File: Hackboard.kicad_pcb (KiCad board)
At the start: 4 copper layers, 100 x 53.3 mm, 74 parts, among them J1 Conn_01x23_Socket, J2 Micro_SD_Card, J3 Conn_01x32_Socket, J4 Conn_01x08_Socket, J5 Conn_01x02_Pin, J6 USB_C_Receptacle_USB2.0_16P, J7 Barrel_Jack_Switch, Q1 NMOS, Q2 NMOS, Q3 NMOS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

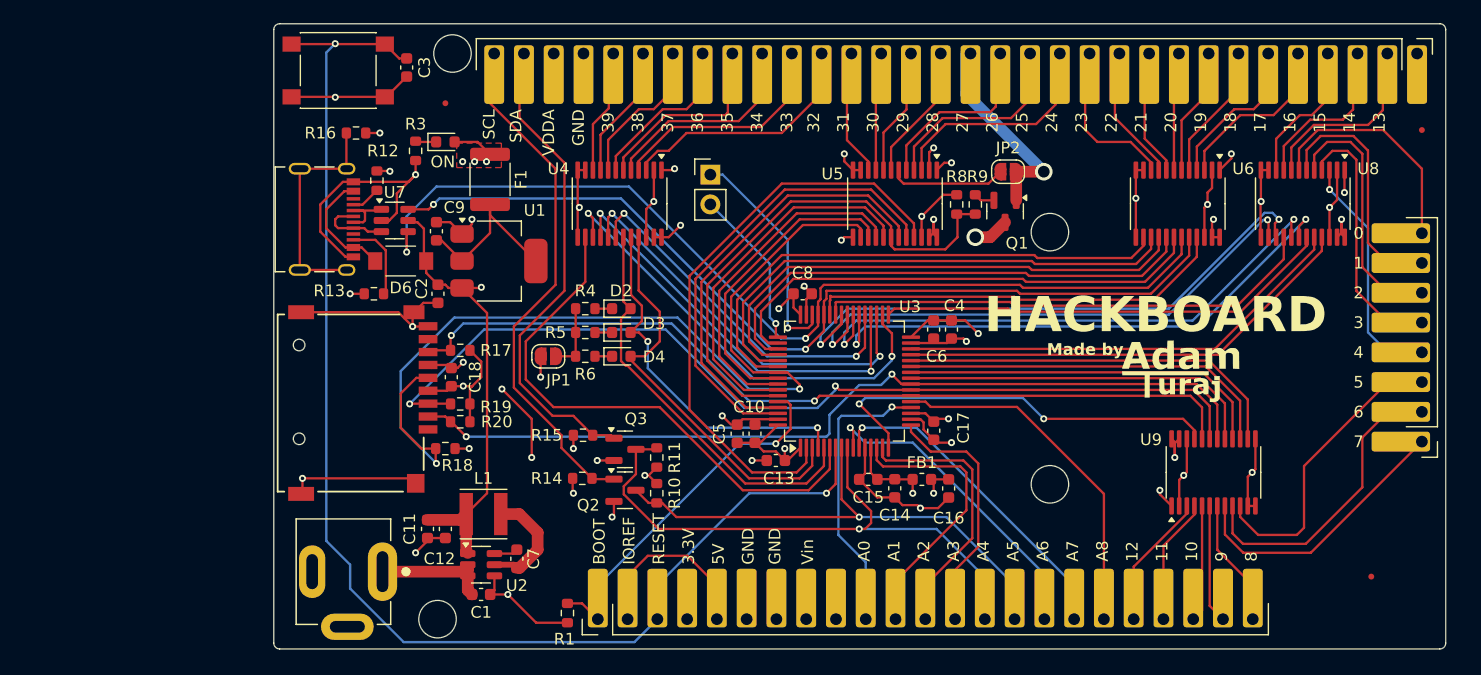
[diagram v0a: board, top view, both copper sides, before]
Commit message: Make changes to header, align headers and holes, start tracing
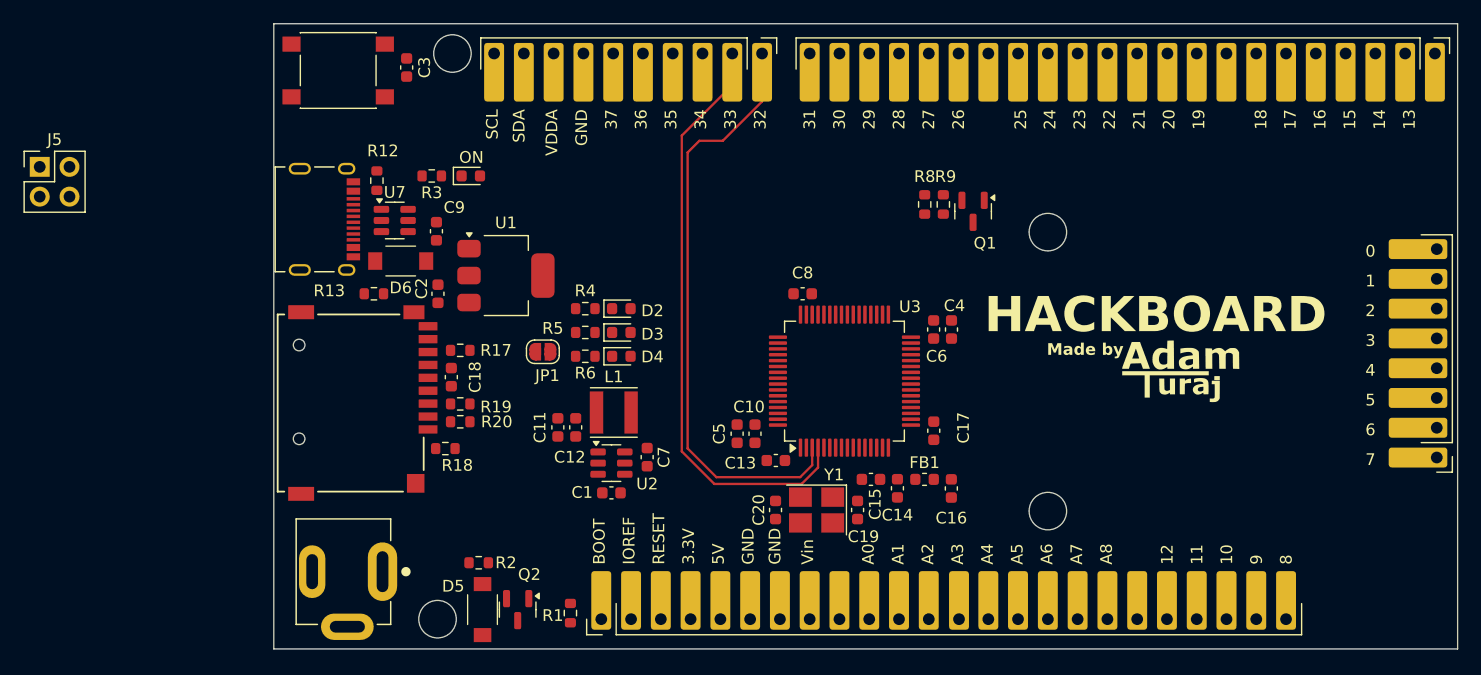
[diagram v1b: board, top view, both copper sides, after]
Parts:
- removed F1: 500mA, Fuse:Fuse_1812_4532Metric
- removed JP2: Jumper_2_Bridged, Jumper:SolderJumper-2_P1.3mm_Open_RoundedPad1.0x1.5mm
- removed Q3: NMOS, Package_TO_SOT_SMD:SOT-23
- removed R10, R11, R14, R15: 10k, Resistor_SMD:R_0603_1608Metric
- removed R16: 1M, Resistor_SMD:R_0603_1608Metric
- removed REF** (x3): Fiducial_0.5mm_Mask1.5mm, Fiducial:Fiducial_0.5mm_Mask1.5mm
- removed U4, U5, U6, U8, U9: 74LVC4245APW, Package_SO:TSSOP-24_4.4x7.8mm_P0.65mm
- added C19: 10pF, Capacitor_SMD:C_0603_1608Metric, F.Cu at (151.5, 117.0)
- added C20: 10pF, Capacitor_SMD:C_0603_1608Metric, F.Cu at (144.5, 117.0)
- added D5: D_Schottky, DO-221AC:VSSAF3L63HM3, F.Cu at (119.5, 125.5)
- added J8: Conn_01x22, Headers:PinSocket_1x22_P2.54mm_Vertical, F.Cu at (200.8, 78.1)
- added R2: 100k, Resistor_SMD:R_0603_1608Metric, F.Cu at (119.2, 121.5)
- added Y1: 48MHz, Oscillator:Oscillator_SMD_Abracon_ASE-4Pin_3.2x2.5mm_HandSoldering, F.Cu at (148.0, 117.0)
- C9: value 22uF -> 4.7uF
- J1: value Conn_01x23_Socket -> Conn_01x24; footprint Connector_PinHeader_2.54mm:PinHeader_1x23_P2.54mm_Vertical -> Headers:PinSocket_1x24_P2.54mm_Vertical
- J3: value Conn_01x32_Socket -> Conn_01x10; footprint Connector_PinHeader_2.54mm:PinHeader_1x32_P2.54mm_Vertical -> Headers:PinSocket_1x10_P2.54mm_Vertical
- J4: value Conn_01x08_Socket -> Conn_01x08; footprint Connector_PinHeader_2.54mm:PinHeader_1x08_P2.54mm_Vertical -> Headers:PinSocket_1x08_P2.54mm_Vertical
- J5: value Conn_01x02_Pin -> Conn_02x02_Counter_Clockwise; footprint Connector_PinHeader_2.54mm:PinHeader_1x02_P2.54mm_Vertical -> Connector_PinHeader_2.54mm:PinHeader_2x02_P2.54mm_Vertical
- R3, R4, R5, R6: value 220R -> 240R
- U1: value AMS1117-3.3 -> AP7361C-33E
- moved J5 57.2 mm to (81.7, 87.7)
- moved J3 55.9 mm to (143.4, 78.1)
- moved L1 14.1 mm to (130.7, 108.7)
- moved C1 14.1 mm to (130.5, 115.5)
- moved C12 14.1 mm to (127.5, 110.0)
- moved C7 14.1 mm to (133.5, 112.5)
- moved U2 14.1 mm to (130.5, 113.0)
- moved C11 14.1 mm to (125.9, 110.0)
- moved Q2 13.7 mm to (122.5, 125.5), turned to -90 degrees
- moved D1 3.62 mm to (118.5, 88.5)
- moved Q1 2.73 mm to (161.4, 91.5)
- moved R8 2.73 mm to (157.2, 90.9)
- moved R9 2.73 mm to (158.8, 90.9)
- moved R3 2.54 mm to (115.2, 88.5), turned to 180 degrees
- moved H2 2.29 mm to (167.7, 117.1)
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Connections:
- C9 pad 2: Net-(U1-VO) -> +3V3
- J1 pad 19: PWM_12_O -> unconnected-(J1-Pin_19-Pad19)
- J1 pad 20: SD_MISO_11_O -> PWM_12
- J1 pad 21: SD_MOSI_10_O -> SD_MISO_11
- J1 pad 22: SD_CS_9_O -> SD_MOSI_10
- J1 pad 23: GPIO_8_O -> SD_CS_9
- J3 pad 10: GPIO_34_O -> GPIO_32
- J3 pad 5: GPIO_39_O -> SPI_SCK_37
- J3 pad 6: SPI_SCK_38_O -> SPI_MOSI_36
- J3 pad 7: SPI_MOSI_37_O -> SPI_MISO_35
- J3 pad 8: SPI_MISO_36_O -> SPI_CS_PWM_34
- J3 pad 9: SPI_CS_PWM_35_O -> GPIO_33
- J4 pad 1: PWM_7_O -> PWM_7
- J4 pad 2: PWM_6_O -> PWM_6
- J4 pad 3: GPIO_5_O -> GPIO_5
- J4 pad 4: PWM_4_O -> PWM_4
- J4 pad 5: PWM_3_O -> PWM_3
- J4 pad 6: PWM_2_O -> PWM_2
- J4 pad 7: PWM_1_O -> PWM_1
- J4 pad 8: PWM_0_O -> PWM_0
- J5 pad 1: SW_SWDIO -> +3V3
- J5 pad 2: SW_SWCLK -> SW_SWDIO
- J6 pad S1: Net-(J6-SHIELD) -> GND
- J7 pad 2: GND -> Net-(D5-A)
- J7 pad 3: GND -> Net-(D5-A)
- Q1 pad 1: PWM_27_O -> PWM_27
- Q2 pad 1: SCL -> GND
- Q2 pad 2: VDDA -> Net-(D5-K)
- Q2 pad 3: I2C_SCL_A5 -> Net-(D5-A)
- R12 pad 2: +3V3 -> GND
- R13 pad 2: +3V3 -> GND
- U1 pad 1: GND -> +5V
- U1 pad 2: Net-(U1-VO) -> GND
- U1 pad 3: +5V -> +3V3
- U3 pad 34: SPI_SCK_38 -> SPI_SCK_37
- U3 pad 35: SPI_MISO_36 -> SPI_MISO_35
- U3 pad 36: SPI_MOSI_37 -> SPI_MOSI_36
- U3 pad 37: SPI_CS_PWM_35 -> SPI_CS_PWM_34
- U3 pad 5: GPIO_34 -> Net-(U3-PH0)
- U3 pad 6: GPIO_39 -> Net-(U3-PH1)
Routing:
- net +5V: track 247.9 -> 0.00 mm, vias 8 -> 0
- net GND: track 173.7 -> 0.00 mm, vias 28 -> 0
- net VCC: track 115.4 -> 0.00 mm, vias 1 -> 0
- net RESET: track 111.9 -> 0.00 mm, vias 2 -> 0
- net VDDA: track 99.3 -> 0.00 mm, vias 6 -> 0
- net SD_SCK_31: track 84.9 -> 0.00 mm, vias 2 -> 0
- net USB_DP_18: track 83.9 -> 0.00 mm, vias 2 -> 0
- net SD_MOSI_10: track 81.6 -> 0.00 mm, vias 2 -> 0
- net USB_DM_17: track 79.4 -> 0.00 mm, vias 2 -> 0
- net SD_CS_9: track 75.2 -> 0.00 mm, vias 2 -> 0
- net SD_MISO_11: track 73.9 -> 0.00 mm, vias 2 -> 0
- net +3V3: track 59.2 -> 0.00 mm, vias 17 -> 0
- net I2C_SDA_A4: track 51.9 -> 0.00 mm, vias 1 -> 0
- net GPIO_24: track 50.2 -> 0.00 mm
- net PWM_14: track 49.5 -> 0.00 mm, vias 2 -> 0
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- removed copper zone on F.Cu, net +3V3
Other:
- board size 100 x 53.3 mm -> 101 x 53.3 mm
- board text removed: "38"
- board text removed: "39"

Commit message: Adjust pinout, start tracing
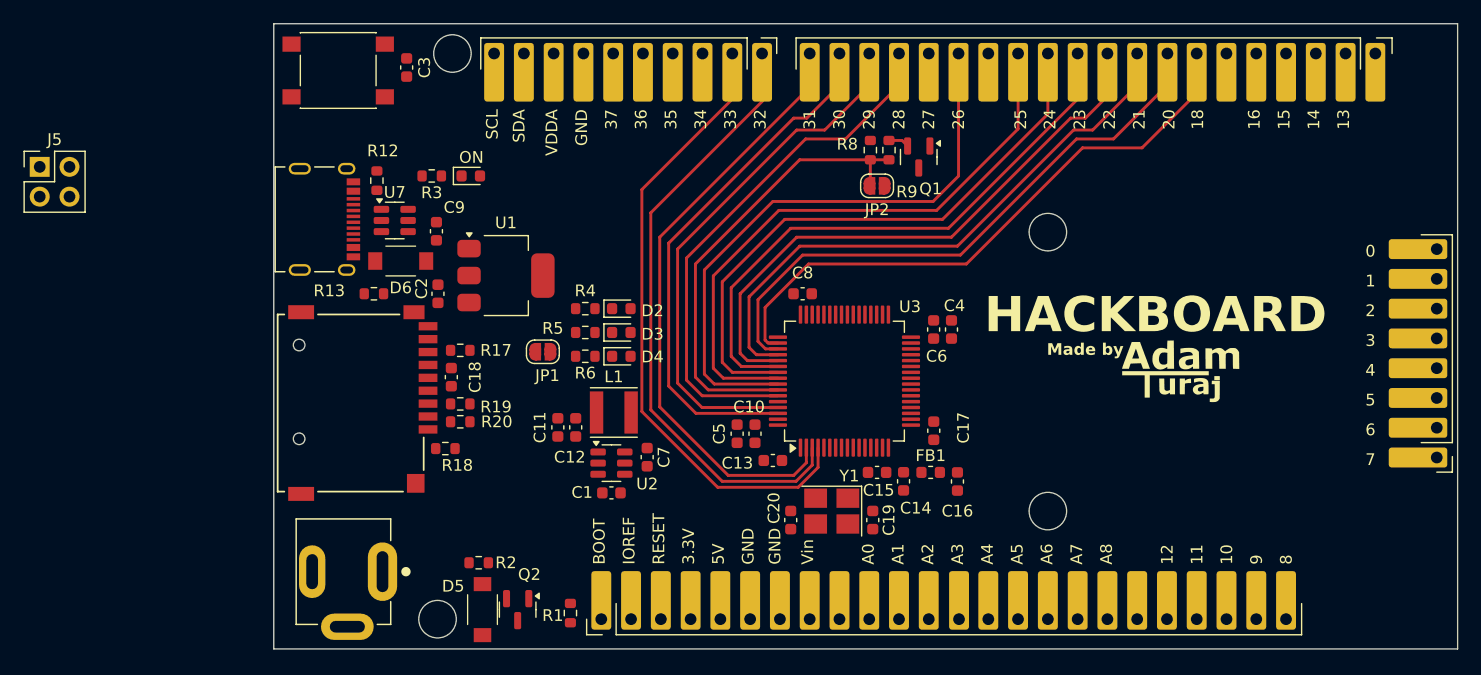
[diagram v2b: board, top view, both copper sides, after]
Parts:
- added JP2: Jumper_2_Bridged, Jumper:SolderJumper-2_P1.3mm_Open_RoundedPad1.0x1.5mm, F.Cu at (153.2, 89.3)
- J8: value Conn_01x22 -> Conn_01x20; footprint Headers:PinSocket_1x22_P2.54mm_Vertical -> Headers:PinSocket_1x20_P2.54mm_Vertical
- moved Q1 6.56 mm to (156.7, 86.9)
- moved R8 6.56 mm to (152.6, 86.3)
- moved R9 6.56 mm to (154.2, 86.3)
- moved J8 5.08 mm to (195.7, 78.1)
- moved C19 1.55 mm to (152.8, 117.9)
- moved C20 1.55 mm to (145.8, 117.9)
- moved Y1 1.30 mm to (149.3, 117.1)
- moved C16 0.79 mm to (160.0, 114.6)
- moved C14 0.79 mm to (155.4, 114.6)
- moved C15 0.79 mm to (153.2, 113.8)
- moved FB1 0.79 mm to (157.7, 113.8)
- moved C13 0.25 mm to (144.3, 112.8)
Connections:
- net GPIO_22 renamed GPIO_20
- net GPIO_23 renamed GPIO_21
- net PWM_19 renamed PWM_17
- net SPI_CS_PWM_34 renamed SPI_CS_PWM_32
- net SPI_MISO_35 renamed SPI_MISO_33
- net SPI_MOSI_36 renamed SPI_MOSI_34
- net SPI_SCK_37 renamed SPI_SCK_35
- net UART_RX_21 renamed UART_RX_19
- net UART_TX_20 renamed UART_TX_18
- J3 pad 1: SCL -> I2C_SCL_A5
- J3 pad 10: GPIO_32 -> GPIO_30
- J3 pad 2: SDA -> I2C_SDA_A4
- J3 pad 9: GPIO_33 -> GPIO_31
- J8 pad 1: SD_SCK_31 -> GPIO_29
- J8 pad 16: USB_DP_18 -> PWM_16
- J8 pad 17: USB_DM_17 -> PWM_15
- J8 pad 18: PWM_16 -> PWM_14
- J8 pad 19: PWM_15 -> PWM_13
- J8 pad 2: PWM_30 -> CAN_TX_28
- J8 pad 20: PWM_14 -> unconnected-(J8-Pin_20-Pad20)
- J8 pad 3: PWM_29 -> CAN_RX_27
- J8 pad 4: PWM_28 -> PWM_26
- J8 pad 5: PWM_27 -> PWM_25_O
- J8 pad 6: CAN_RX_26 -> PWM_24
- J8 pad 8: CAN_TX_25 -> PWM_23
- J8 pad 9: GPIO_24 -> SD_SCK_22
- Q1 pad 1: PWM_27 -> PWM_25_O
- R8 pad 1: PWM_27 -> PWM_25
- R9 pad 2: PWM_27 -> PWM_25
- U3 pad 16: PWM_12 -> PWM_8
- U3 pad 2: GPIO_24 -> GPIO_29
- U3 pad 22: SD_MISO_11 -> SD_MISO_9
- U3 pad 24: SD_CS_9 -> SD_CS_11
- U3 pad 25: GPIO_8 -> GPIO_12
- U3 pad 3: GPIO_32 -> GPIO_30
- U3 pad 4: GPIO_33 -> GPIO_31
- U3 pad 40: PWM_15 -> PWM_13
- U3 pad 42: PWM_13 -> PWM_15
- U3 pad 44: USB_DM_17 -> USB_DM
- U3 pad 45: USB_DP_18 -> USB_DP
- U3 pad 55: SD_SCK_31 -> SD_SCK_22
- U3 pad 56: PWM_30 -> PWM_23
- U3 pad 57: PWM_29 -> PWM_24
- U3 pad 58: PWM_28 -> PWM_25
- U3 pad 59: PWM_27 -> PWM_26
- U3 pad 61: CAN_RX_26 -> CAN_RX_27
- U3 pad 62: CAN_TX_25 -> CAN_TX_28
- U7 pad 4: USB_DP_18 -> USB_DP
- U7 pad 6: USB_DM_17 -> USB_DM
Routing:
- net GPIO_31: track 0.00 -> 53.8 mm
- net GPIO_30: track 0.00 -> 52.7 mm
- net GPIO_29: track 0.00 -> 52.1 mm
- net PWM_17: track 0.00 -> 51.8 mm
- net PWM_23: track 0.00 -> 51.4 mm
- net GPIO_32: track 51.1 -> 0.00 mm
- net PWM_24: track 0.00 -> 51.0 mm
- net SD_SCK_22: track 0.00 -> 50.8 mm
- net GPIO_33: track 50.8 -> 0.00 mm
- net UART_TX_18: track 0.00 -> 50.7 mm
- net GPIO_20: track 0.00 -> 50.5 mm
- net UART_RX_19: track 0.00 -> 50.3 mm
- net GPIO_21: track 0.00 -> 50.3 mm
- net PWM_26: track 0.00 -> 45.7 mm
- net CAN_RX_27: track 0.00 -> 45.7 mm
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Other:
- board text removed: "17"
- board text removed: "19"

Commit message: Continue routing
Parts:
- moved J5 46.7 mm to (128.3, 91.2)
- moved C9 8.68 mm to (118.6, 101.3), turned to 180 degrees
- moved L1 6.90 mm to (125.0, 112.5)
- moved C11 6.90 mm to (120.2, 113.8)
- moved C12 6.90 mm to (121.7, 113.8)
- moved U2 6.90 mm to (124.8, 116.8)
- moved C1 6.90 mm to (124.8, 119.4)
- moved C7 6.90 mm to (127.8, 116.3)
- moved C2 6.31 mm to (117.3, 92.5), turned to 180 degrees
- moved JP2 4.01 mm to (150.4, 86.5), turned to 90 degrees
- moved R6 3.06 mm to (126.0, 105.9)
- moved R4 3.06 mm to (126.0, 101.9)
- moved R5 3.06 mm to (126.0, 103.9)
- moved D4 3.06 mm to (129.1, 105.9)
- moved D2 3.06 mm to (129.1, 101.9)
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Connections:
- D2 pad 2: GPIO_34 -> GPIO_31
- D3 pad 2: GPIO_33 -> GPIO_30
- D4 pad 2: GPIO_32 -> GPIO_29
- J1 pad 2: +5V -> +3V3
- J1 pad 5: +5V -> +3V3
- J2 pad 5: SD_SCK_31 -> SD_SCK_22
- R18 pad 2: SD_SCK_31 -> SD_SCK_22
- U3 pad 16: PWM_8 -> PWM_12
- U3 pad 22: SD_MISO_9 -> SD_MISO_11
- U3 pad 24: SD_CS_11 -> SD_CS_9
- U3 pad 25: GPIO_12 -> GPIO_8
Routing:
- net SD_CS_9: track 0.00 -> 104.0 mm, vias 0 -> 2
- net RESET: track 0.00 -> 100.0 mm, vias 0 -> 3
- net SD_MOSI_10: track 0.00 -> 98.6 mm, vias 0 -> 2
- net SD_MISO_11: track 0.00 -> 90.3 mm, vias 0 -> 2
- net PWM_13: track 0.00 -> 58.6 mm
- net PWM_14: track 0.00 -> 57.1 mm
- net PWM_0: track 0.00 -> 53.0 mm
- net SD_SCK_22: track 50.8 -> 102.6 mm, vias 0 -> 2
- net PWM_15: track 0.00 -> 51.1 mm
- net PWM_1: track 0.00 -> 51.0 mm
- net PWM_16: track 0.00 -> 49.5 mm
- net PWM_7: track 0.00 -> 47.9 mm
- net PWM_6: track 0.00 -> 47.0 mm
- net PWM_2: track 0.00 -> 47.0 mm
- net GPIO_5: track 0.00 -> 46.2 mm
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
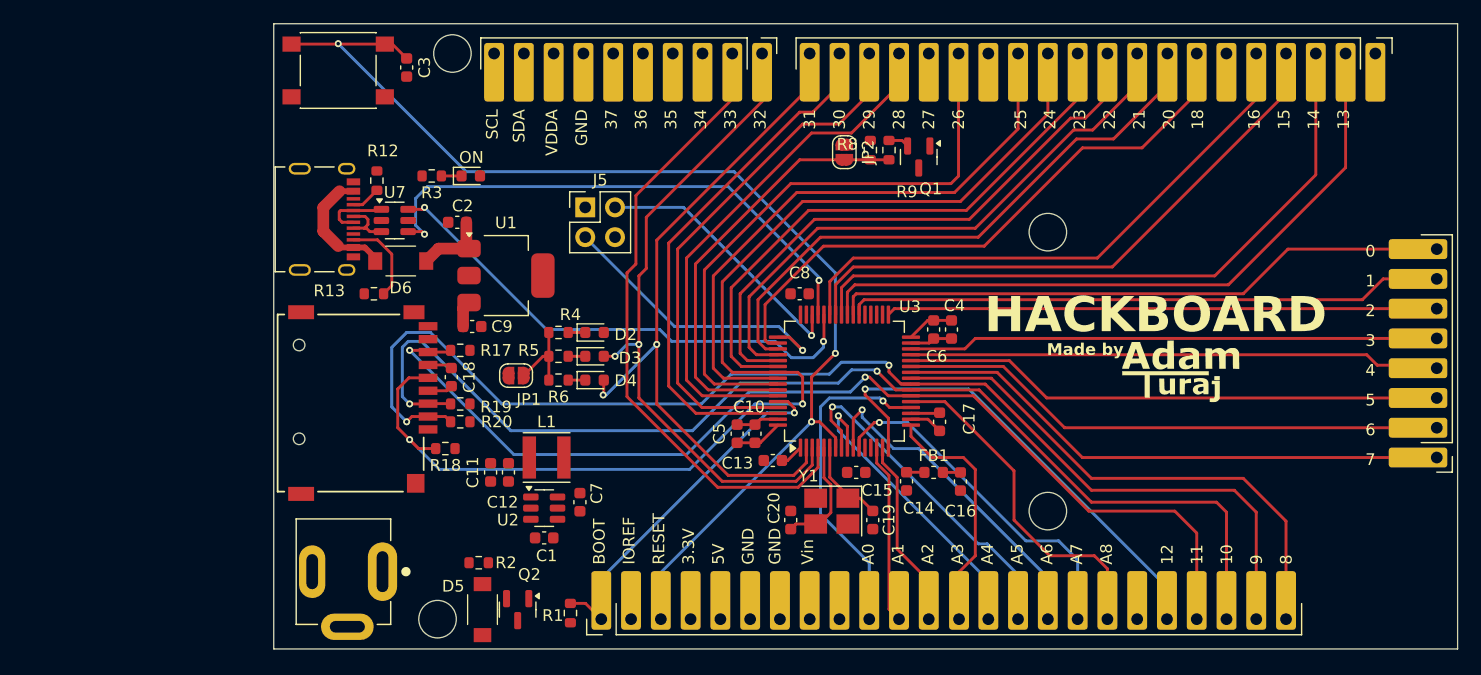
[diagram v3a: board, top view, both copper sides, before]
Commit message: Continue tracing, switch MOSFET's and diodes
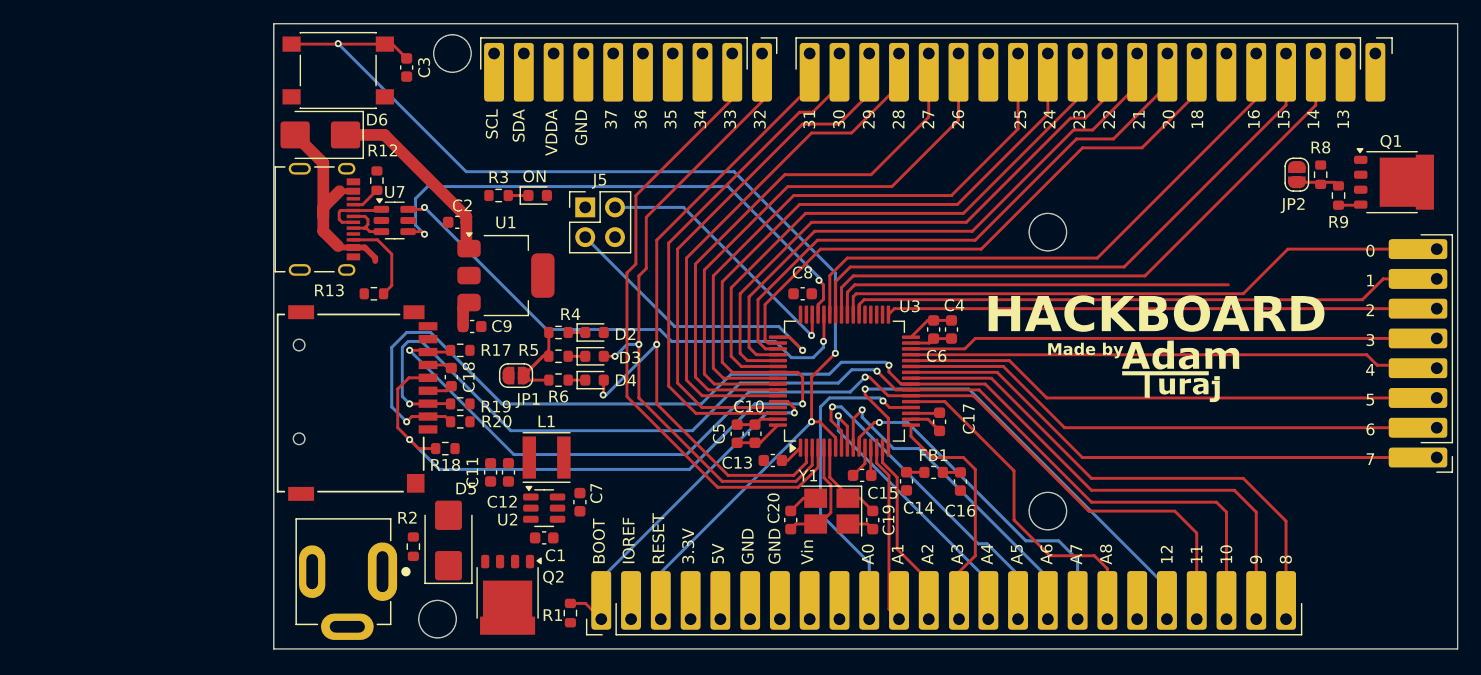
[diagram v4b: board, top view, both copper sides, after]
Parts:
- D5, D6: footprint DO-221AC:VSSAF3L63HM3 -> Diode_SMD:D_SMB
- Q1, Q2: value NMOS -> PSMN041; footprint Package_TO_SOT_SMD:SOT-23 -> Package_TO_SOT_SMD:LFPAK56
- moved Q1 40.4 mm to (197.1, 89.0), turned to 0 degrees
- moved JP2 38.7 mm to (189.0, 88.4)
- moved R9 38.5 mm to (192.5, 90.2), turned to 90 degrees
- moved R8 38.5 mm to (191.0, 88.4)
- moved D6 12.8 mm to (105.7, 85.0)
- moved D5 6.57 mm to (116.6, 119.6), turned to 90 degrees
- moved D1 5.95 mm to (124.2, 90.2)
- moved R3 5.95 mm to (120.9, 90.2)
- moved R2 5.74 mm to (113.6, 120.1), turned to 90 degrees
- moved Q2 1.67 mm to (121.6, 124.1)
- moved C15 0.57 mm to (151.9, 114.0)
- moved C8 0.25 mm to (146.8, 98.6)
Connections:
- J8 pad 19: PWM_13 -> PWM_13_O
- J8 pad 5: PWM_25_O -> PWM_25
- JP2 pad 1: PWM_25 -> PWM_13
- JP2 pad 2: PWM_25_O -> PWM_13_O
- Q1 pad 1: PWM_25_O -> PWM_13_O
- R8 pad 1: PWM_25 -> PWM_13
- R9 pad 2: PWM_25 -> PWM_13
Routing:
- net PWM_13: track 58.6 -> 38.4 mm
- net PWM_25: track 37.3 -> 47.7 mm
- net +5V: track 6.43 -> 16.0 mm
- net Net-(D6-A): track 10.8 -> 18.8 mm
- net GND: track 12.2 -> 19.9 mm
- net PWM_14: track 57.1 -> 53.6 mm
- net Net-(JP1-B): track 6.89 -> 9.70 mm
- net PWM_24: track 51.0 -> 48.2 mm
- net VDDA: track 1.53 -> 3.91 mm
- net PWM_15: track 51.1 -> 51.9 mm

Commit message: Finish tracing
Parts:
- moved R2 2.04 mm to (113.3, 118.1)
- moved D5 1.59 mm to (117.9, 118.6), turned to 0 degrees
- moved Q2 0.26 mm to (121.7, 124.3), turned to 0 degrees
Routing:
- net VCC: track 0.00 -> 130.6 mm, vias 0 -> 1
- net GND: track 19.9 -> 94.1 mm, vias 0 -> 46
- net VDDA: track 3.91 -> 59.1 mm, vias 0 -> 2
- net I2C_SCL_A5: track 29.5 -> 81.6 mm, vias 1 -> 2
- net I2C_SDA_A4: track 25.7 -> 77.4 mm, vias 1 -> 2
- net SPI_CS_PWM_32: track 0.00 -> 44.2 mm, vias 0 -> 1
- net SPI_MISO_33: track 0.00 -> 43.8 mm, vias 0 -> 1
- net SPI_MOSI_34: track 0.00 -> 43.2 mm, vias 0 -> 1
- net SPI_SCK_35: track 0.00 -> 41.7 mm, vias 0 -> 1
- net +5V: track 16.0 -> 49.1 mm
- net Net-(D5-A): track 0.00 -> 26.5 mm
- net PWM_13_O: track 0.00 -> 24.3 mm
- net +3V3: track 18.6 -> 38.7 mm, vias 0 -> 12
- net Net-(D5-K): track 0.00 -> 19.9 mm
- net PWM_13: track 38.4 -> 49.5 mm
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- added copper zone on F.Cu, net +3V3
- added copper zone on F.Cu, net GND
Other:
- board text added: "17"
- board text added: "19"
- board text removed: "36"
- board text removed: "37"
